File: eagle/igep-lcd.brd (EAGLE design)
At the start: 99.9 x 59.6 mm, 72 parts, among them IC1 LM1117IMPX-3.3, U1 SN74LVC8T245PW, U2 SN74LVC8T245PW, U3 SN74LVC8T245PW, U4 SN74LVC8T245PW

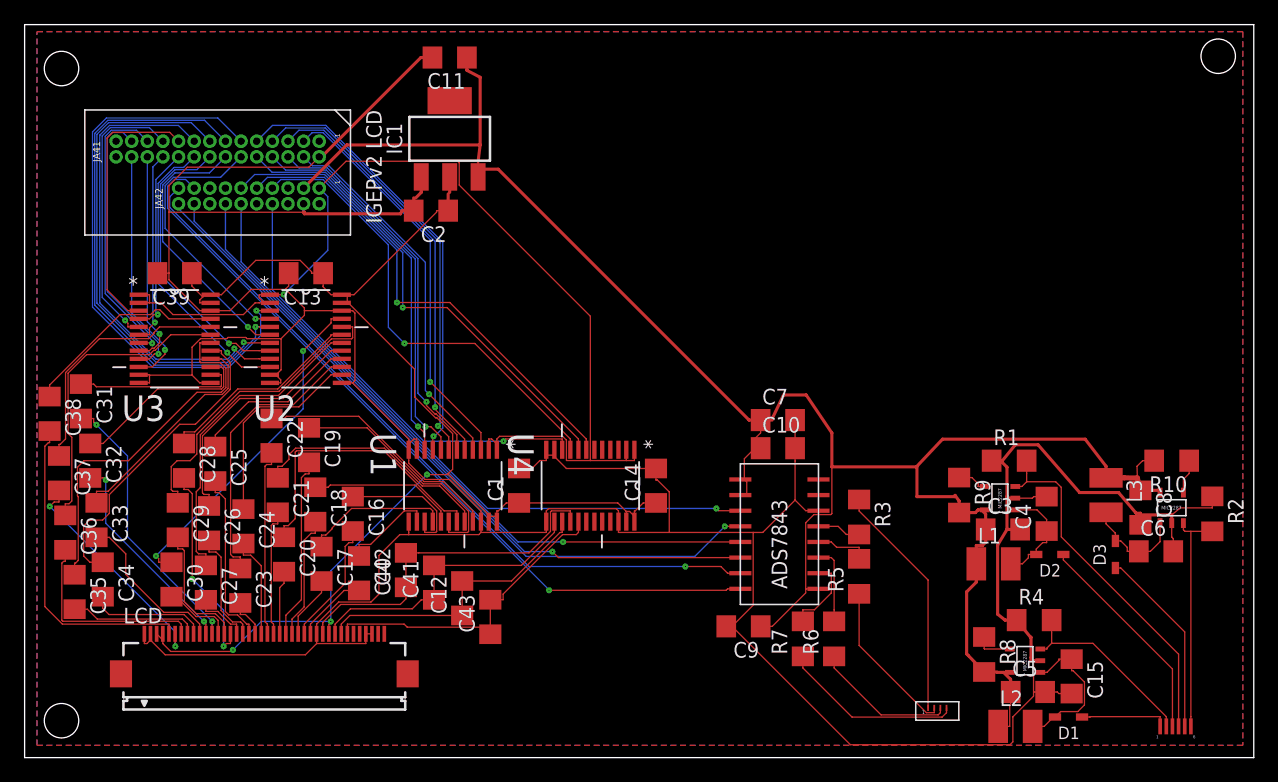
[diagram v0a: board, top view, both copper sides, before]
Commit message: Added workaround for different design rules
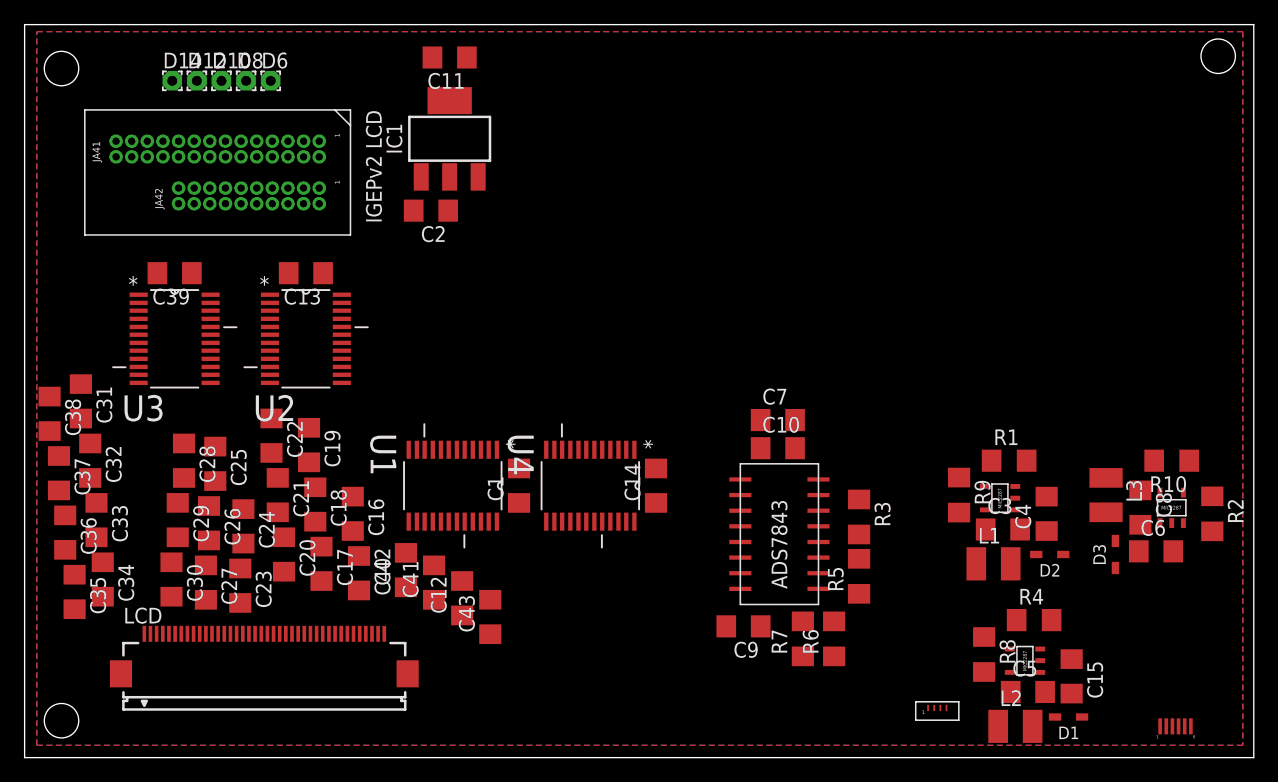
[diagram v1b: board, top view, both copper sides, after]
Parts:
- added D10, D12, D14, D6, D8: (no value), wirepad:1,6/0,8
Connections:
- net LCD_DATA10: now also D10.1
- net LCD_DATA12: now also D12.1
- net LCD_DATA14: now also D14.1
- net LCD_DATA17: no longer LCD.6
- net LCD_DATA19: no longer LCD.8
- net LCD_DATA21: no longer LCD.10
- net LCD_DATA23: no longer LCD.12
- net LCD_DATA6: now also D6.1
- net LCD_DATA8: now also D8.1
- net LCD_DATA9: no longer LCD.14
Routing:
- net N$2: track 325.8 -> 0.00 mm
- net N$35: track 159.9 -> 0.00 mm
- net N$36: track 108.1 -> 0.00 mm, vias 3 -> 0
- net N$4: track 84.6 -> 0.00 mm, vias 1 -> 0
- net N$1: track 63.9 -> 0.00 mm, vias 1 -> 0
- net N$7: track 60.6 -> 0.00 mm, vias 1 -> 0
- net N$27: track 58.8 -> 0.00 mm, vias 1 -> 0
- net N$26: track 57.1 -> 0.00 mm, vias 1 -> 0
- net N$25: track 55.4 -> 0.00 mm, vias 1 -> 0
- net N$20: track 53.7 -> 0.00 mm, vias 1 -> 0
- net IGEP_LCD_DATA8: track 47.6 -> 0.00 mm, vias 1 -> 0
- net IGEP_LCD_DATA10: track 43.8 -> 0.00 mm, vias 1 -> 0
- net IGEP_LCD_DATA12: track 40.9 -> 0.00 mm, vias 1 -> 0
- net PCLK: track 40.3 -> 0.00 mm, vias 1 -> 0
- net DEN: track 39.3 -> 0.00 mm, vias 1 -> 0
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
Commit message: Added routing
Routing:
- net N$2: track 0.00 -> 343.1 mm, vias 0 -> 1
- net N$35: track 0.00 -> 160.2 mm
- net N$36: track 0.00 -> 108.6 mm, vias 0 -> 3
- net LCD_DATA6: track 0.00 -> 81.2 mm, vias 0 -> 1
- net LCD_DATA10: track 0.00 -> 67.4 mm, vias 0 -> 2
- net N$4: track 0.00 -> 65.7 mm, vias 0 -> 2
- net N$1: track 0.00 -> 63.7 mm, vias 0 -> 2
- net LCD_DATA8: track 0.00 -> 61.6 mm, vias 0 -> 1
- net N$27: track 0.00 -> 61.5 mm, vias 0 -> 1
- net LCD_DATA12: track 0.00 -> 61.0 mm, vias 0 -> 1
- net N$7: track 0.00 -> 60.6 mm, vias 0 -> 1
- net N$26: track 0.00 -> 56.7 mm, vias 0 -> 1
- net LCD_DATA14: track 0.00 -> 55.9 mm, vias 0 -> 2
- net N$25: track 0.00 -> 54.2 mm, vias 0 -> 1
- net N$20: track 0.00 -> 53.9 mm, vias 0 -> 1
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
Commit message: Revert to 286b264bb1132dfa6f59ae8d288566ef804c77dd
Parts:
- removed D10, D12, D14, D6, D8: (no value), wirepad:1,6/0,8
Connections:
- net LCD_DATA10: no longer D10.1
- net LCD_DATA12: no longer D12.1
- net LCD_DATA14: no longer D14.1
- net LCD_DATA17: now also LCD.6
- net LCD_DATA19: now also LCD.8
- net LCD_DATA21: now also LCD.10
- net LCD_DATA23: now also LCD.12
- net LCD_DATA6: no longer D6.1
- net LCD_DATA8: no longer D8.1
- net LCD_DATA9: now also LCD.14
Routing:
- net LCD_DATA6: track 81.2 -> 10.2 mm, vias 1 -> 0
- net LCD_DATA8: track 61.6 -> 5.68 mm, vias 1 -> 0
- net LCD_DATA14: track 55.9 -> 3.26 mm, vias 2 -> 0
- net LCD_DATA12: track 61.0 -> 9.44 mm, vias 1 -> 0
- net LCD_DATA10: track 67.4 -> 16.7 mm
- net LCD_DATA23: track 0.00 -> 22.5 mm, vias 0 -> 2
- net N$4: track 65.7 -> 84.6 mm, vias 2 -> 1
- net LCD_DATA17: track 0.00 -> 18.5 mm, vias 0 -> 2
- net N$2: track 343.1 -> 325.8 mm, vias 1 -> 0
- net IGEP_LCD_DATA8: track 31.9 -> 47.6 mm, vias 3 -> 1
- net N$17: track 44.7 -> 29.2 mm
- net N$18: track 34.1 -> 19.3 mm
- net LCD_DATA21: track 0.00 -> 13.1 mm
- net LCD_DATA9: track 0.00 -> 10.6 mm
- net LCD_DATA19: track 0.00 -> 10.5 mm
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
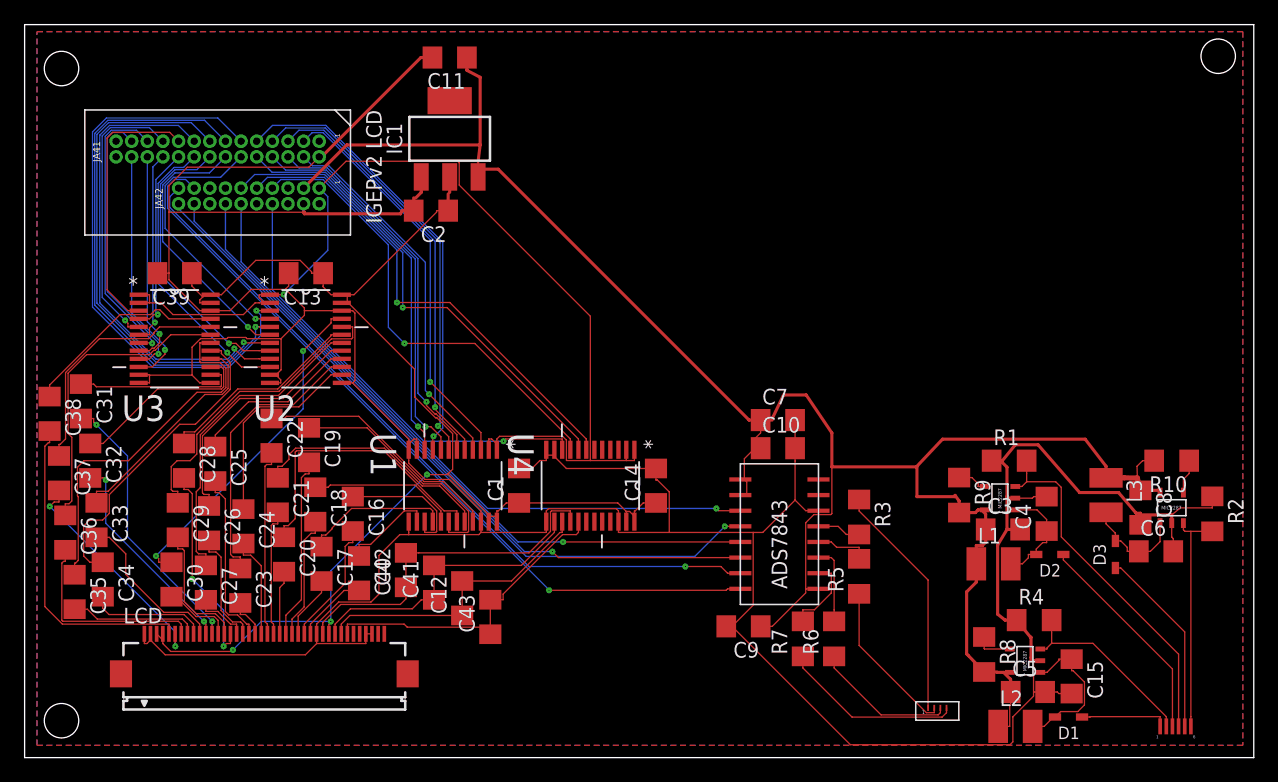
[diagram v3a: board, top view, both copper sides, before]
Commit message: Fixed postion testpads in schematic
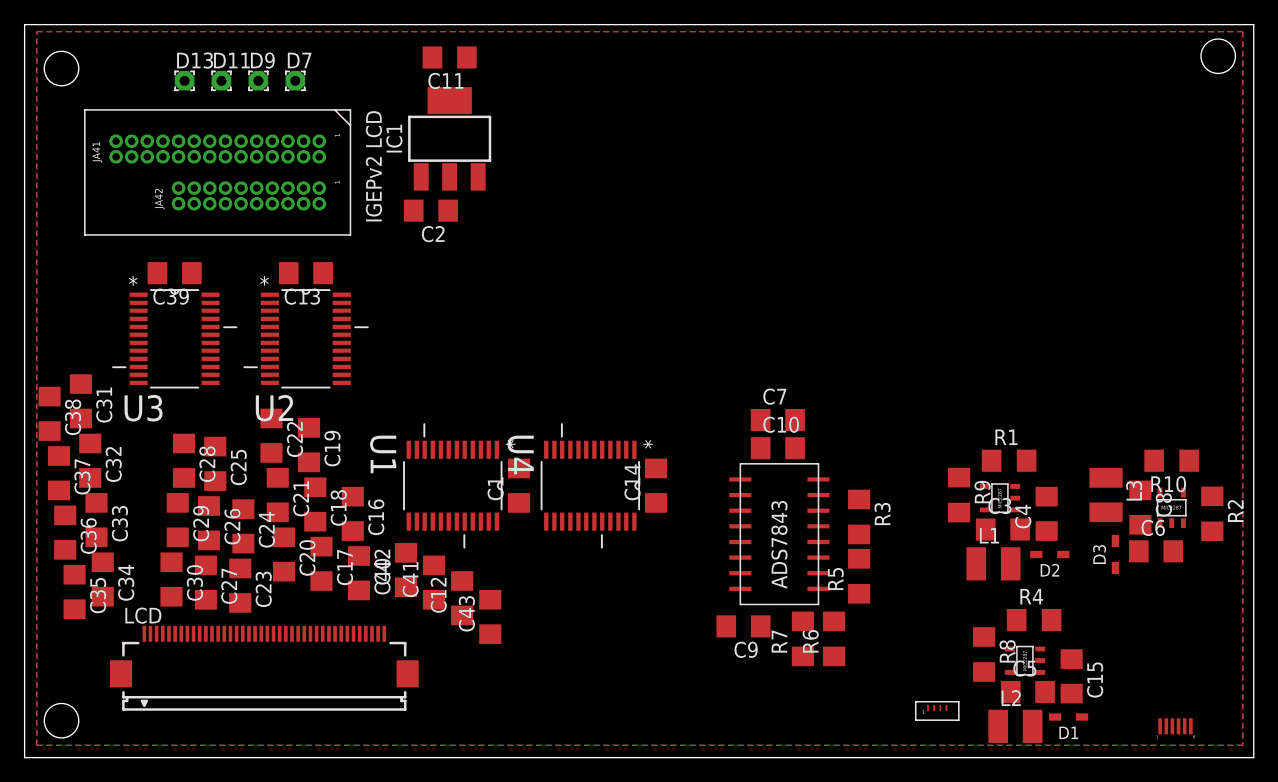
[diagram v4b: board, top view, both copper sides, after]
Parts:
- added D11, D13, D7, D9: (no value), wirepad:1,6/0,8
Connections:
- net IGEP_LCD_DATA11: now also D11.1; no longer U$1.D11
- net IGEP_LCD_DATA13: now also D13.1; no longer U$1.D13
- net IGEP_LCD_DATA7: now also D7.1; no longer U$1.D7
- net IGEP_LCD_DATA9: now also D9.1; no longer U$1.D9
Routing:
- net N$2: track 325.8 -> 0.00 mm
- net N$35: track 159.9 -> 0.00 mm
- net N$36: track 108.1 -> 0.00 mm, vias 3 -> 0
- net N$4: track 84.6 -> 0.00 mm, vias 1 -> 0
- net N$1: track 63.9 -> 0.00 mm, vias 1 -> 0
- net N$7: track 60.6 -> 0.00 mm, vias 1 -> 0
- net N$27: track 58.8 -> 0.00 mm, vias 1 -> 0
- net N$26: track 57.1 -> 0.00 mm, vias 1 -> 0
- net N$25: track 55.4 -> 0.00 mm, vias 1 -> 0
- net N$20: track 53.7 -> 0.00 mm, vias 1 -> 0
- net IGEP_LCD_DATA8: track 47.6 -> 0.00 mm, vias 1 -> 0
- net IGEP_LCD_DATA10: track 43.8 -> 0.00 mm, vias 1 -> 0
- net IGEP_LCD_DATA12: track 40.9 -> 0.00 mm, vias 1 -> 0
- net PCLK: track 40.3 -> 0.00 mm, vias 1 -> 0
- net DEN: track 39.3 -> 0.00 mm, vias 1 -> 0
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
